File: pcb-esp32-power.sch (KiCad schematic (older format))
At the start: 12 parts, among them J1 C-OBD-II-16M, J2 Bus_Connector, J3 Conn_01x02, U1 STEPDOWN12_5

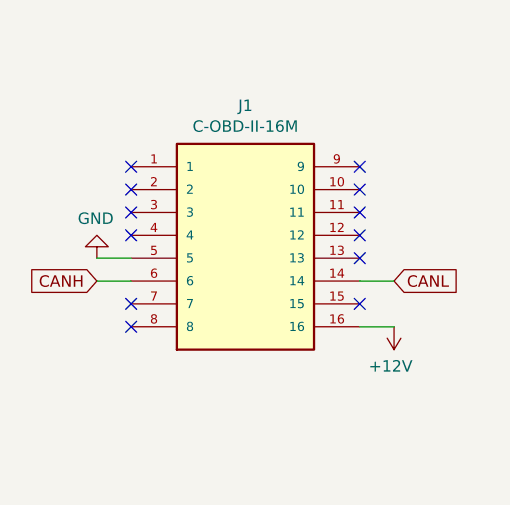
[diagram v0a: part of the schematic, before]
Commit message: OBD Pin 4 & 5 an Masse
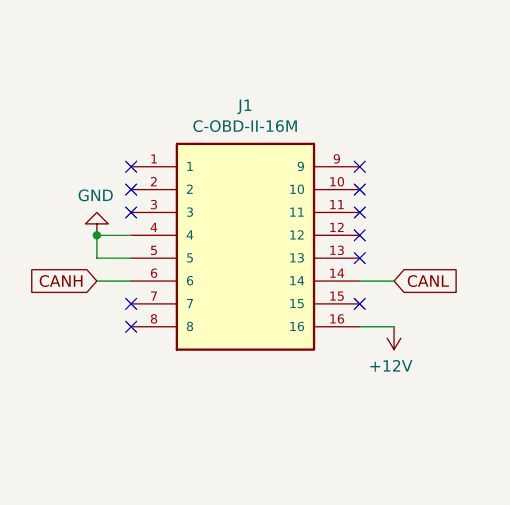
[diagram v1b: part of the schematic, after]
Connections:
- net GND: now also J1.4
- no-connect marks 34 -> 33
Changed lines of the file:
@@
 L power:GND #PWR01
 U 1 1 6103C4CA
-P 1100 1600
-F 0 "#PWR01" H 1100 1350 50  0001 C CNN
-F 1 "GND" H 1105 1427 50  0000 C CNN
-F 2 "" H 1100 1600 50  0001 C CNN
-F 3 "" H 1100 1600 50  0001 C CNN
-	1    1100 1600
+P 1100 1500
+F 0 "#PWR01" H 1100 1250 50  0001 C CNN
+F 1 "GND" H 1105 1327 50  0000 C CNN
+F 2 "" H 1100 1500 50  0001 C CNN
+F 3 "" H 1100 1500 50  0001 C CNN
+	1    1100 1500
 	-1   0    0    1
 $EndComp
@@
 NoConn ~ 1250 1300
 NoConn ~ 1250 1400
-NoConn ~ 1250 1500
 NoConn ~ 1250 1800
 NoConn ~ 1250 1900
@@
 Wire Wire Line
 	6950 5200 6950 5250
+Wire Wire Line
+	1250 1500 1100 1500
+Wire Wire Line
+	1100 1600 1100 1500
+Connection ~ 1100 1500
 $EndSCHEMATC

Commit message: Erste Version mit LTC4091
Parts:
- removed U1: STEPDOWN12_5, StepDownBreakout:StepDownBreakout, symbol stepdown12_5:STEPDOWN12_5
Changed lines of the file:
@@
 $Descr A4 11693 8268
 encoding utf-8
-Sheet 1 4
+Sheet 1 3
 Title ""
 Date ""
@@
 $EndDescr
 $Comp
-L power:+12V #PWR04
-U 1 1 60DA8AE4
-P 3350 1400
-F 0 "#PWR04" H 3350 1250 50  0001 C CNN
-F 1 "+12V" H 3365 1573 50  0000 C CNN
-F 2 "" H 3350 1400 50  0001 C CNN
-F 3 "" H 3350 1400 50  0001 C CNN
-	1    3350 1400
-	1    0    0    -1
-$EndComp
-$Comp
-L power:GND #PWR05
-U 1 1 60DA924D
-P 3350 1700
-F 0 "#PWR05" H 3350 1450 50  0001 C CNN
-F 1 "GND" H 3355 1527 50  0000 C CNN
-F 2 "" H 3350 1700 50  0001 C CNN
-F 3 "" H 3350 1700 50  0001 C CNN
-	1    3350 1700
-	1    0    0    -1
-$EndComp
-Wire Wire Line
-	3350 1700 3350 1600
-Wire Wire Line
-	3350 1600 3500 1600
-Wire Wire Line
-	3500 1400 3350 1400
-Text GLabel 4400 1400 2    50   Input ~ 0
-5VIN
-$Comp
-L power:GND #PWR07
-U 1 1 60DB30D1
-P 4400 1700
-F 0 "#PWR07" H 4400 1450 50  0001 C CNN
-F 1 "GND" H 4405 1527 50  0000 C CNN
-F 2 "" H 4400 1700 50  0001 C CNN
-F 3 "" H 4400 1700 50  0001 C CNN
-	1    4400 1700
-	1    0    0    -1
-$EndComp
-Wire Wire Line
-	4250 1400 4400 1400
-Wire Wire Line
-	4250 1600 4400 1600
-Wire Wire Line
-	4400 1600 4400 1700
-$Comp
 L power:PWR_FLAG #FLG02
 U 1 1 60DBE6F2
@@
 $EndComp
 $Comp
-L power:PWR_FLAG #FLG04
-U 1 1 60D74F1F
-P 6550 6900
-F 0 "#FLG04" H 6550 6975 50  0001 C CNN
-F 1 "PWR_FLAG" H 6550 7073 50  0000 C CNN
-F 2 "" H 6550 6900 50  0001 C CNN
-F 3 "~" H 6550 6900 50  0001 C CNN
-	1    6550 6900
-	1    0    0    -1
-$EndComp
-$Comp
-L power:+3.3V #PWR012
-U 1 1 60D75745
-P 6550 6900
-F 0 "#PWR012" H 6550 6750 50  0001 C CNN
-F 1 "+3.3V" H 6565 7073 50  0000 C CNN
-F 2 "" H 6550 6900 50  0001 C CNN
-F 3 "" H 6550 6900 50  0001 C CNN
-	1    6550 6900
-	-1   0    0    1
-$EndComp
-$Comp
 L Connector_Generic:Conn_01x02 J3
 U 1 1 60EFB4F7
@@
 Wire Wire Line
 	7400 3350 7500 3350
-$Comp
-L stepdown12_5:STEPDOWN12_5 U1
-U 1 1 60F48B5B
-P 3850 1800
-F 0 "U1" H 3825 1185 50  0000 C CNN
-F 1 "STEPDOWN12_5" H 3825 1276 50  0000 C CNN
-F 2 "StepDownBreakout:StepDownBreakout" H 3850 1800 50  0001 C CNN
-F 3 "" H 3850 1800 50  0001 C CNN
-	1    3850 1800
-	-1   0    0    1
-$EndComp
 Text GLabel 5950 1300 0    50   Input ~ 0
 5VIN
@@
 L power:GND #PWR01
 U 1 1 6103C4CA
-P 1100 1500
-F 0 "#PWR01" H 1100 1250 50  0001 C CNN
-F 1 "GND" H 1105 1327 50  0000 C CNN
-F 2 "" H 1100 1500 50  0001 C CNN
-F 3 "" H 1100 1500 50  0001 C CNN
-	1    1100 1500
+P 1100 1600
+F 0 "#PWR01" H 1100 1350 50  0001 C CNN
+F 1 "GND" H 1105 1427 50  0000 C CNN
+F 2 "" H 1100 1600 50  0001 C CNN
+F 3 "" H 1100 1600 50  0001 C CNN
+	1    1100 1600
 	-1   0    0    1
 $EndComp
@@
 NoConn ~ 2250 1300
 NoConn ~ 2250 1200
-$Sheet
-S 9800 650  1200 850
-U 612652A3
-F0 "TP4054" 50
-F1 "tp4054/tp4054.sch" 50
-$EndSheet
-$Sheet
-S 9900 1750 1100 950
-U 612B5E8A
-F0 "SY8008" 50
-F1 "sy8008/sy8008.sch" 50
-$EndSheet
 Wire Wire Line
 	2500 3900 2600 3900
@@
 Wire Wire Line
 	6950 5200 6950 5250
-Wire Wire Line
-	1250 1500 1100 1500
-Wire Wire Line
-	1100 1600 1100 1500
-Connection ~ 1100 1500
+$Sheet
+S 9900 4200 1100 850
+U 6172D804
+F0 "LTC4091" 50
+F1 "ltc4091/ltc4091.sch" 50
+$EndSheet
+Wire Wire Line
+	1250 1500 1250 1600
+Connection ~ 1250 1600
 $EndSCHEMATC

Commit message: Keine "Handsolder" Footprints mehr
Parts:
- CP1: renamed from CP5; footprint Capacitor_Tantalum_SMD:CP_EIA-6032-28_Kemet-C_Pad2.25x2.35mm_HandSolder -> Capacitor_Tantalum_SMD:CP_EIA-6032-28_Kemet-C
- CP2: footprint Capacitor_Tantalum_SMD:CP_EIA-6032-28_Kemet-C_Pad2.25x2.35mm_HandSolder -> Capacitor_Tantalum_SMD:CP_EIA-6032-28_Kemet-C
- R1, R2: footprint Resistor_SMD:R_0603_1608Metric_Pad0.98x0.95mm_HandSolder -> Resistor_SMD:R_0603_1608Metric
- R3: renamed from R18; footprint Resistor_SMD:R_0603_1608Metric_Pad0.98x0.95mm_HandSolder -> Resistor_SMD:R_0603_1608Metric
- R4: renamed from R3; footprint Resistor_SMD:R_0603_1608Metric_Pad0.98x0.95mm_HandSolder -> Resistor_SMD:R_0603_1608Metric
- R5: renamed from R4; footprint Resistor_SMD:R_0603_1608Metric_Pad0.98x0.95mm_HandSolder -> Resistor_SMD:R_0603_1608Metric
- renumbered D2 to D1
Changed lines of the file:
@@
 $EndComp
 $Comp
-L power:+12V #PWR010
+L power:+12V #PWR06
 U 1 1 60DBEB3A
 P 5750 6900
-F 0 "#PWR010" H 5750 6750 50  0001 C CNN
+F 0 "#PWR06" H 5750 6750 50  0001 C CNN
 F 1 "+12V" H 5765 7073 50  0000 C CNN
 F 2 "" H 5750 6900 50  0001 C CNN
@@
 $EndComp
 $Comp
-L power:GND #PWR011
+L power:GND #PWR09
 U 1 1 60DBF487
 P 6150 6900
-F 0 "#PWR011" H 6150 6650 50  0001 C CNN
+F 0 "#PWR09" H 6150 6650 50  0001 C CNN
 F 1 "GND" H 6155 6727 50  0000 C CNN
 F 2 "" H 6150 6900 50  0001 C CNN
@@
 F 0 "R1" H 6220 1496 50  0000 L CNN
 F 1 "200k" H 6220 1405 50  0000 L CNN
-F 2 "Resistor_SMD:R_0603_1608Metric_Pad0.98x0.95mm_HandSolder" V 6080 1450 50  0001 C CNN
+F 2 "Resistor_SMD:R_0603_1608Metric" V 6080 1450 50  0001 C CNN
 F 3 "~" H 6150 1450 50  0001 C CNN
 	1    6150 1450
@@
 F 0 "R2" H 6220 1896 50  0000 L CNN
 F 1 "390k" H 6220 1805 50  0000 L CNN
-F 2 "Resistor_SMD:R_0603_1608Metric_Pad0.98x0.95mm_HandSolder" V 6080 1850 50  0001 C CNN
+F 2 "Resistor_SMD:R_0603_1608Metric" V 6080 1850 50  0001 C CNN
 F 3 "~" H 6150 1850 50  0001 C CNN
 	1    6150 1850
@@
 	6150 1650 6150 1700
 $Comp
-L power:GND #PWR09
+L power:GND #PWR08
 U 1 1 60F64C82
 P 6150 2000
-F 0 "#PWR09" H 6150 1750 50  0001 C CNN
+F 0 "#PWR08" H 6150 1750 50  0001 C CNN
 F 1 "GND" H 6155 1827 50  0000 C CNN
 F 2 "" H 6150 2000 50  0001 C CNN
@@
 	3600 4000 3700 4000
 $Comp
-L power:GND #PWR06
+L power:GND #PWR04
 U 1 1 60F7A061
 P 3700 3400
-F 0 "#PWR06" H 3700 3150 50  0001 C CNN
+F 0 "#PWR04" H 3700 3150 50  0001 C CNN
 F 1 "GND" H 3705 3227 50  0000 C CNN
 F 2 "" H 3700 3400 50  0001 C CNN
@@
 $EndComp
 $Comp
-L Device:R R3
+L Device:R R4
 U 1 1 6131E154
 P 7600 1450
-F 0 "R3" H 7670 1496 50  0000 L CNN
+F 0 "R4" H 7670 1496 50  0000 L CNN
 F 1 "470k" H 7670 1405 50  0000 L CNN
-F 2 "Resistor_SMD:R_0603_1608Metric_Pad0.98x0.95mm_HandSolder" V 7530 1450 50  0001 C CNN
+F 2 "Resistor_SMD:R_0603_1608Metric" V 7530 1450 50  0001 C CNN
 F 3 "~" H 7600 1450 50  0001 C CNN
 	1    7600 1450
@@
 $EndComp
 $Comp
-L Device:R R4
+L Device:R R5
 U 1 1 6131E8A9
 P 7600 1850
-F 0 "R4" H 7670 1896 50  0000 L CNN
+F 0 "R5" H 7670 1896 50  0000 L CNN
 F 1 "470k" H 7670 1805 50  0000 L CNN
-F 2 "Resistor_SMD:R_0603_1608Metric_Pad0.98x0.95mm_HandSolder" V 7530 1850 50  0001 C CNN
+F 2 "Resistor_SMD:R_0603_1608Metric" V 7530 1850 50  0001 C CNN
 F 3 "~" H 7600 1850 50  0001 C CNN
 	1    7600 1850
@@
 NoConn ~ 4650 4000
 $Comp
-L power:+BATT #PWR08
+L power:+BATT #PWR05
 U 1 1 61364414
 P 5300 6900
-F 0 "#PWR08" H 5300 6750 50  0001 C CNN
+F 0 "#PWR05" H 5300 6750 50  0001 C CNN
 F 1 "+BATT" H 5315 7073 50  0000 C CNN
 F 2 "" H 5300 6900 50  0001 C CNN
@@
 $EndSheet
 $Comp
-L power:+3.3V #PWR0103
+L power:+3.3V #PWR010
 U 1 1 6135B72B
 P 6450 3100
-F 0 "#PWR0103" H 6450 2950 50  0001 C CNN
+F 0 "#PWR010" H 6450 2950 50  0001 C CNN
 F 1 "+3.3V" H 6465 3273 50  0000 C CNN
 F 2 "" H 6450 3100 50  0001 C CNN
@@
 F 0 "CP2" H 6568 3296 50  0000 L CNN
 F 1 "22uF" H 6568 3205 50  0000 L CNN
-F 2 "Capacitor_Tantalum_SMD:CP_EIA-6032-28_Kemet-C_Pad2.25x2.35mm_HandSolder" H 6488 3100 50  0001 C CNN
+F 2 "Capacitor_Tantalum_SMD:CP_EIA-6032-28_Kemet-C" H 6488 3100 50  0001 C CNN
 F 3 "~" H 6450 3250 50  0001 C CNN
 	1    6450 3250
@@
 $EndComp
 $Comp
-L power:GND #PWR0104
+L power:GND #PWR011
 U 1 1 6135CC65
 P 6450 3400
-F 0 "#PWR0104" H 6450 3150 50  0001 C CNN
+F 0 "#PWR011" H 6450 3150 50  0001 C CNN
 F 1 "GND" H 6455 3227 50  0000 C CNN
 F 2 "" H 6450 3400 50  0001 C CNN
@@
 5VOUT
 $Comp
-L Device:CP CP5
+L Device:CP CP1
 U 1 1 6136F84A
 P 6000 3250
-F 0 "CP5" H 6118 3296 50  0000 L CNN
+F 0 "CP1" H 6118 3296 50  0000 L CNN
 F 1 "22uF" H 6118 3205 50  0000 L CNN
-F 2 "Capacitor_Tantalum_SMD:CP_EIA-6032-28_Kemet-C_Pad2.25x2.35mm_HandSolder" H 6038 3100 50  0001 C CNN
+F 2 "Capacitor_Tantalum_SMD:CP_EIA-6032-28_Kemet-C" H 6038 3100 50  0001 C CNN
 F 3 "~" H 6000 3250 50  0001 C CNN
 	1    6000 3250
@@
 $EndComp
 $Comp
-L power:GND #PWR0105
+L power:GND #PWR07
 U 1 1 6136FEB6
 P 6000 3400
-F 0 "#PWR0105" H 6000 3150 50  0001 C CNN
+F 0 "#PWR07" H 6000 3150 50  0001 C CNN
 F 1 "GND" H 6005 3227 50  0000 C CNN
 F 2 "" H 6000 3400 50  0001 C CNN
@@
 LED
 $Comp
-L Device:R R18
+L Device:R R3
 U 1 1 61363F18
 P 6950 4700
-F 0 "R18" H 7020 4746 50  0000 L CNN
+F 0 "R3" H 7020 4746 50  0000 L CNN
 F 1 "1K" H 7020 4655 50  0000 L CNN
-F 2 "Resistor_SMD:R_0603_1608Metric_Pad0.98x0.95mm_HandSolder" V 6880 4700 50  0001 C CNN
+F 2 "Resistor_SMD:R_0603_1608Metric" V 6880 4700 50  0001 C CNN
 F 3 "~" H 6950 4700 50  0001 C CNN
 	1    6950 4700
@@
 $EndComp
 $Comp
-L Device:LED D2
+L Device:LED D1
 U 1 1 613648CD
 P 6950 5050
-F 0 "D2" V 6989 4932 50  0000 R CNN
+F 0 "D1" V 6989 4932 50  0000 R CNN
 F 1 "LED green" V 6898 4932 50  0000 R CNN
 F 2 "LED_SMD:LED_0805_2012Metric_Pad1.15x1.40mm_HandSolder" H 6950 5050 50  0001 C CNN
@@
 $EndComp
 $Comp
-L power:GND #PWR0106
+L power:GND #PWR012
 U 1 1 61365CD6
 P 6950 5250
-F 0 "#PWR0106" H 6950 5000 50  0001 C CNN
+F 0 "#PWR012" H 6950 5000 50  0001 C CNN
 F 1 "GND" H 6955 5077 50  0000 C CNN
 F 2 "" H 6950 5250 50  0001 C CNN

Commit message: Footprint Änderungen Kondensatoren & Induktoren
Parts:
- removed CP1, CP2: 22uF, Capacitor_Tantalum_SMD:CP_EIA-6032-28_Kemet-C, symbol Device:CP
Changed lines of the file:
@@
 F1 "ltc3530/ltc3530.sch" 50
 $EndSheet
-$Comp
-L power:+3.3V #PWR010
-U 1 1 6135B72B
-P 6450 3100
-F 0 "#PWR010" H 6450 2950 50  0001 C CNN
-F 1 "+3.3V" H 6465 3273 50  0000 C CNN
-F 2 "" H 6450 3100 50  0001 C CNN
-F 3 "" H 6450 3100 50  0001 C CNN
-	1    6450 3100
-	1    0    0    -1
-$EndComp
-$Comp
-L Device:CP CP2
-U 1 1 6135C742
-P 6450 3250
-F 0 "CP2" H 6568 3296 50  0000 L CNN
-F 1 "22uF" H 6568 3205 50  0000 L CNN
-F 2 "Capacitor_Tantalum_SMD:CP_EIA-6032-28_Kemet-C" H 6488 3100 50  0001 C CNN
-F 3 "~" H 6450 3250 50  0001 C CNN
-	1    6450 3250
-	1    0    0    -1
-$EndComp
-$Comp
-L power:GND #PWR011
-U 1 1 6135CC65
-P 6450 3400
-F 0 "#PWR011" H 6450 3150 50  0001 C CNN
-F 1 "GND" H 6455 3227 50  0000 C CNN
-F 2 "" H 6450 3400 50  0001 C CNN
-F 3 "" H 6450 3400 50  0001 C CNN
-	1    6450 3400
-	1    0    0    -1
-$EndComp
-Text GLabel 5900 3050 0    50   Input ~ 0
-5VOUT
-$Comp
-L Device:CP CP1
-U 1 1 6136F84A
-P 6000 3250
-F 0 "CP1" H 6118 3296 50  0000 L CNN
-F 1 "22uF" H 6118 3205 50  0000 L CNN
-F 2 "Capacitor_Tantalum_SMD:CP_EIA-6032-28_Kemet-C" H 6038 3100 50  0001 C CNN
-F 3 "~" H 6000 3250 50  0001 C CNN
-	1    6000 3250
-	1    0    0    -1
-$EndComp
-$Comp
-L power:GND #PWR07
-U 1 1 6136FEB6
-P 6000 3400
-F 0 "#PWR07" H 6000 3150 50  0001 C CNN
-F 1 "GND" H 6005 3227 50  0000 C CNN
-F 2 "" H 6000 3400 50  0001 C CNN
-F 3 "" H 6000 3400 50  0001 C CNN
-	1    6000 3400
-	1    0    0    -1
-$EndComp
-Wire Wire Line
-	5900 3050 6000 3050
-Wire Wire Line
-	6000 3050 6000 3100
 Text GLabel 2500 4200 0    50   Input ~ 0
 LED
